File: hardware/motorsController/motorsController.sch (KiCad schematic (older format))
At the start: 12 parts, among them J1 batery_connector, J10 batery_connector, J11 Conn_01x04, J2 Screw_Terminal_01x01, J3 Screw_Terminal_01x01, J4 Screw_Terminal_01x01, J5 Screw_Terminal_01x01, J6 Screw_Terminal_01x01, J7 Screw_Terminal_01x01, J8 Screw_Terminal_01x01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

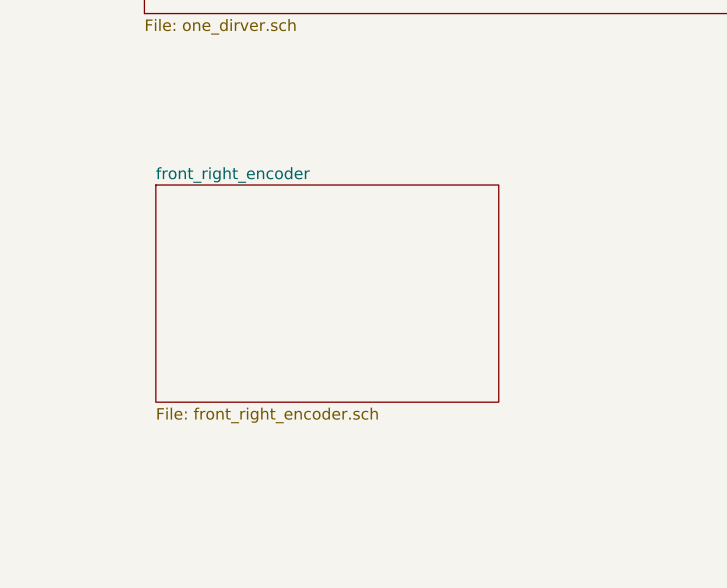
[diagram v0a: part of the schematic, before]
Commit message: layout filters for an encoder
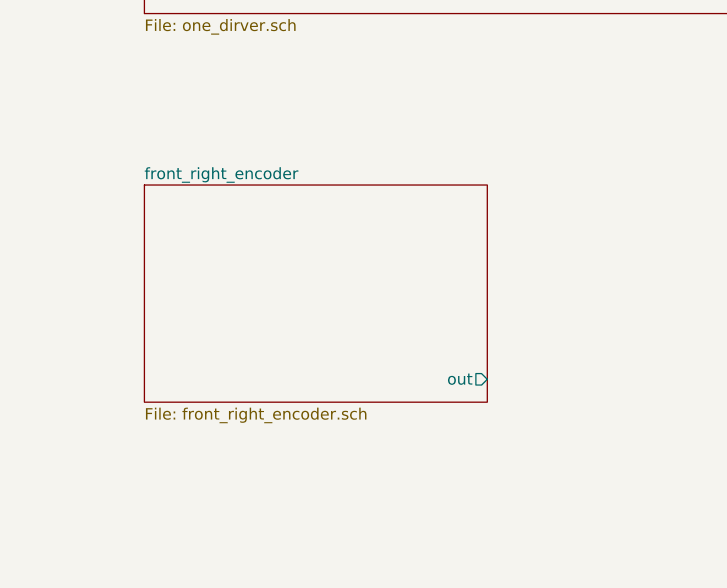
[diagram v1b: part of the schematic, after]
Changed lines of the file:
@@
 $EndComp
 $Sheet
-S 1300 6400 1500 950
+S 1250 6400 1500 950
 U 5FB03879
 F0 "front_right_encoder" 50
 F1 "front_right_encoder.sch" 50
+F2 "out" O R 2750 7250 50
 $EndSheet
 $EndSCHEMATC

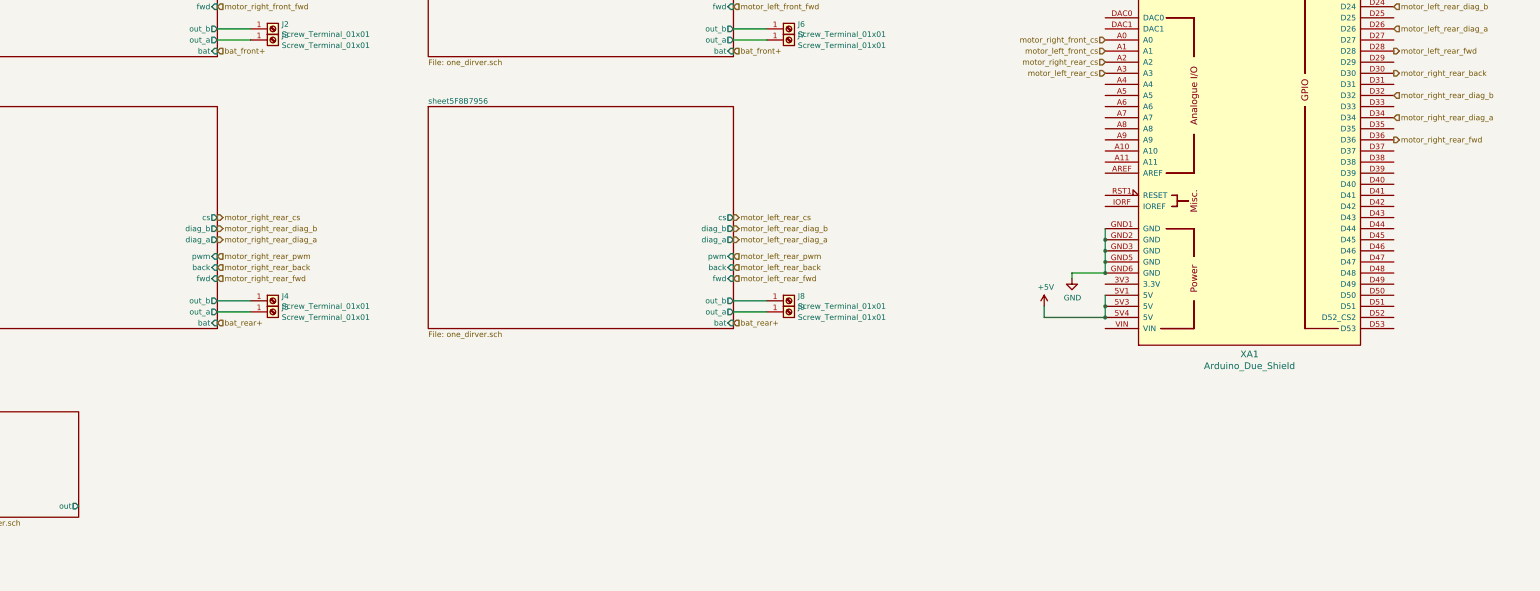
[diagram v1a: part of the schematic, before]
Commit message: connect encoder to arduino
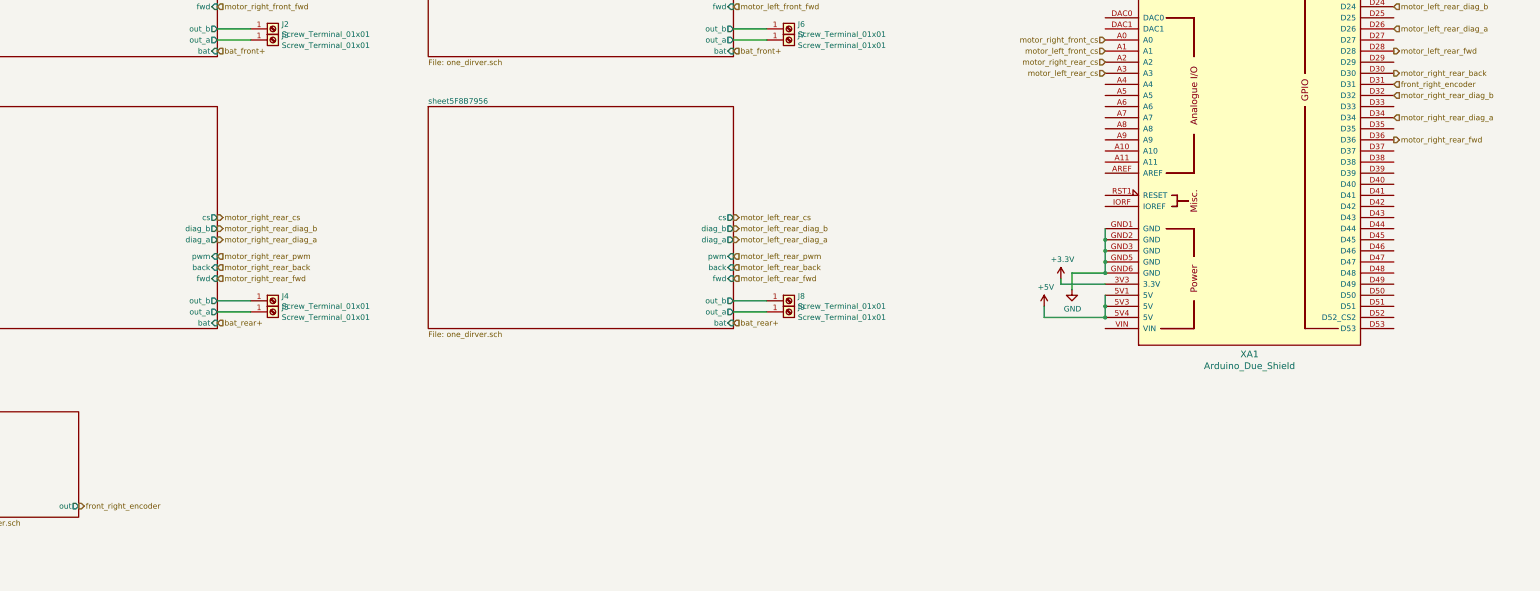
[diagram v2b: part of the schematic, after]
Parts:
- J11: footprint Connector_PinHeader_1.00mm:PinHeader_1x04_P1.00mm_Vertical -> Connector_PinSocket_2.54mm:PinSocket_1x04_P2.54mm_Vertical
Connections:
- net +3V3: now reaches XA1.3V3 (3.3V)
- net front_right_encoder: now reaches XA1.D31
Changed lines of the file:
@@
 L power:GND #PWR0105
 U 1 1 5F7FA8F7
-P 11700 5200
-F 0 "#PWR0105" H 11700 4950 50  0001 C CNN
-F 1 "GND" H 11705 5027 50  0000 C CNN
-F 2 "" H 11700 5200 50  0001 C CNN
-F 3 "" H 11700 5200 50  0001 C CNN
-	1    11700 5200
-	1    0    0    -1
-$EndComp
-Wire Wire Line
-	11700 5200 11700 5150
+P 11700 5300
+F 0 "#PWR0105" H 11700 5050 50  0001 C CNN
+F 1 "GND" H 11705 5127 50  0000 C CNN
+F 2 "" H 11700 5300 50  0001 C CNN
+F 3 "" H 11700 5300 50  0001 C CNN
+	1    11700 5300
+	1    0    0    -1
+$EndComp
+Wire Wire Line
+	11700 5300 11700 5150
 Wire Wire Line
 	11700 5150 12000 5150
@@
 F 0 "J11" H 918 9275 50  0000 C CNN
 F 1 "Conn_01x04" H 918 9366 50  0000 C CNN
-F 2 "Connector_PinHeader_1.00mm:PinHeader_1x04_P1.00mm_Vertical" H 1000 9700 50  0001 C CNN
+F 2 "Connector_PinSocket_2.54mm:PinSocket_1x04_P2.54mm_Vertical" H 1000 9700 50  0001 C CNN
 F 3 "~" H 1000 9700 50  0001 C CNN
 	1    1000 9700
@@
 F2 "out" O R 2750 7250 50
 $EndSheet
+$Comp
+L power:+3.3V #PWR0128
+U 1 1 5FBBD825
+P 11600 5200
+F 0 "#PWR0128" H 11600 5050 50  0001 C CNN
+F 1 "+3.3V" H 11615 5373 50  0000 C CNN
+F 2 "" H 11600 5200 50  0001 C CNN
+F 3 "" H 11600 5200 50  0001 C CNN
+	1    11600 5200
+	1    0    0    -1
+$EndComp
+Wire Wire Line
+	11600 5200 11600 5250
+Wire Wire Line
+	11600 5250 12000 5250
+Text HLabel 2750 7250 2    50   Output ~ 0
+front_right_encoder
+Text HLabel 14600 3450 2    50   Input ~ 0
+front_right_encoder
 $EndSCHEMATC

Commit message: add three more encoders
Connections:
- net front_left_encoder: now reaches XA1.D33
- net rear_right_encoder: now reaches XA1.D35
- net rear_left_encoder: now reaches XA1.D37
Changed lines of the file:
@@
 $Descr A3 16535 11693
 encoding utf-8
-Sheet 1 6
+Sheet 1 9
 Title ""
 Date ""
@@
 Text HLabel 14600 3450 2    50   Input ~ 0
 front_right_encoder
+$Sheet
+S 3650 6400 1500 950
+U 5FBFC472
+F0 "front_left_encoder" 50
+F1 "front_right_encoder.sch" 50
+F2 "out" O R 5150 7250 50
+$EndSheet
+Text HLabel 5150 7250 2    50   Output ~ 0
+front_left_encoder
+Text HLabel 14600 3650 2    50   Input ~ 0
+front_left_encoder
+$Sheet
+S 1250 7750 1500 950
+U 5FC04BEE
+F0 "rear_right_encoder" 50
+F1 "front_right_encoder.sch" 50
+F2 "out" O R 2750 8600 50
+$EndSheet
+Text HLabel 2750 8600 2    50   Output ~ 0
+rear_right_encoder
+$Sheet
+S 3650 7750 1500 950
+U 5FC04BF2
+F0 "rear_left_encoder" 50
+F1 "front_right_encoder.sch" 50
+F2 "out" O R 5150 8600 50
+$EndSheet
+Text HLabel 5150 8600 2    50   Output ~ 0
+rear_left_encoder
+Text HLabel 14600 3850 2    50   Input ~ 0
+rear_right_encoder
+Text HLabel 14600 4050 2    50   Input ~ 0
+rear_left_encoder
 $EndSCHEMATC

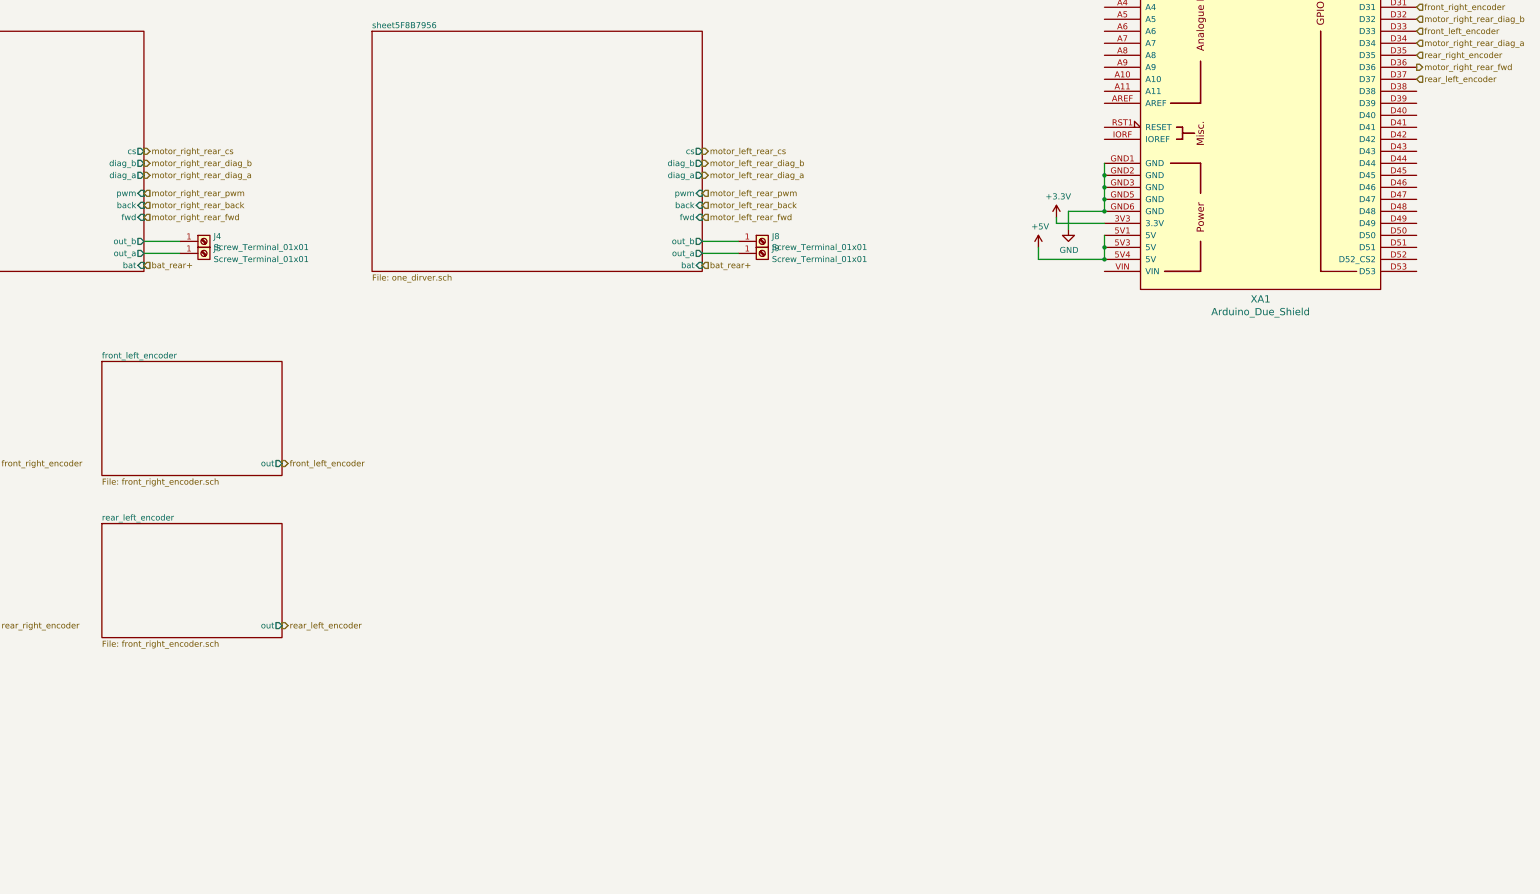
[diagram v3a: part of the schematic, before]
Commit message: add indication leds to schematics
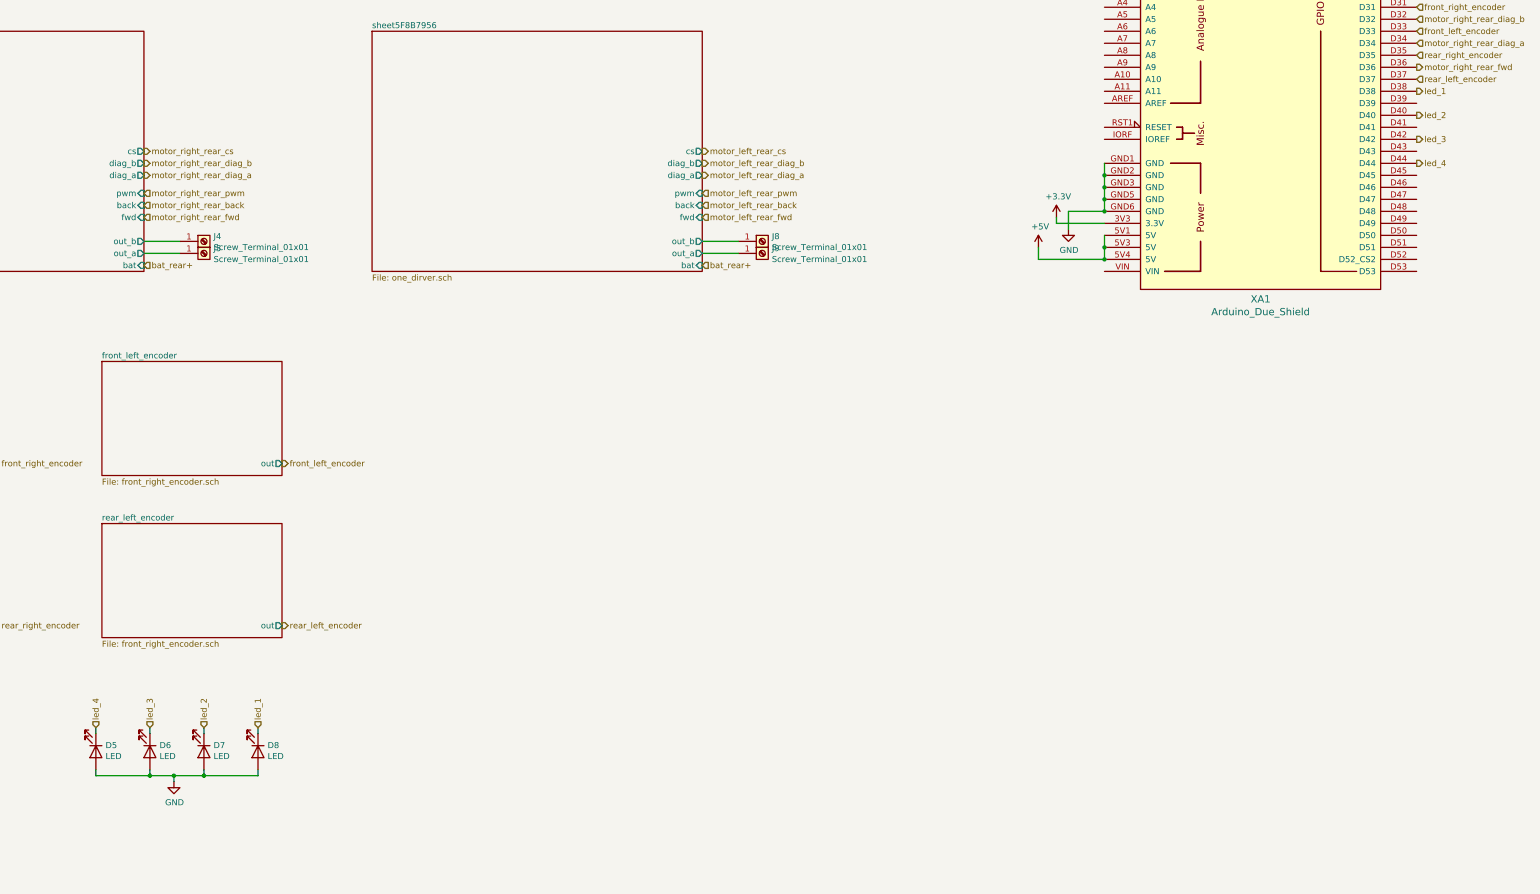
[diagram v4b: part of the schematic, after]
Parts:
- added D5, D6, D7, D8: LED, symbol Device:LED
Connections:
- net GND: now also D5.2 (A), D6.2 (A), D7.2 (A), D8.2 (A)
- net led_1: now reaches XA1.D38
- net led_1: now also D8.1 (K)
- net led_2: now reaches XA1.D40
- net led_2: now also D7.1 (K)
- net led_3: now reaches XA1.D42
- net led_3: now also D6.1 (K)
- net led_4: now reaches XA1.D44
- net led_4: now also D5.1 (K)
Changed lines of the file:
@@
 Text HLabel 14600 4050 2    50   Input ~ 0
 rear_left_encoder
+$Comp
+L Device:LED D5
+U 1 1 5FC19CB9
+P 3600 9650
+F 0 "D5" V 3547 9730 50  0000 L CNN
+F 1 "LED" V 3638 9730 50  0000 L CNN
+F 2 "" H 3600 9650 50  0001 C CNN
+F 3 "~" H 3600 9650 50  0001 C CNN
+	1    3600 9650
+	0    1    1    0
+$EndComp
+$Comp
+L Device:LED D6
+U 1 1 5FC1D350
+P 4050 9650
+F 0 "D6" V 3997 9730 50  0000 L CNN
+F 1 "LED" V 4088 9730 50  0000 L CNN
+F 2 "" H 4050 9650 50  0001 C CNN
+F 3 "~" H 4050 9650 50  0001 C CNN
+	1    4050 9650
+	0    1    1    0
+$EndComp
+$Comp
+L Device:LED D7
+U 1 1 5FC1DB12
+P 4500 9650
+F 0 "D7" V 4447 9730 50  0000 L CNN
+F 1 "LED" V 4538 9730 50  0000 L CNN
+F 2 "" H 4500 9650 50  0001 C CNN
+F 3 "~" H 4500 9650 50  0001 C CNN
+	1    4500 9650
+	0    1    1    0
+$EndComp
+$Comp
+L Device:LED D8
+U 1 1 5FC1E600
+P 4950 9650
+F 0 "D8" V 4897 9730 50  0000 L CNN
+F 1 "LED" V 4988 9730 50  0000 L CNN
+F 2 "" H 4950 9650 50  0001 C CNN
+F 3 "~" H 4950 9650 50  0001 C CNN
+	1    4950 9650
+	0    1    1    0
+$EndComp
+Wire Wire Line
+	3600 9500 3600 9450
+Wire Wire Line
+	4950 9450 4950 9500
+Wire Wire Line
+	4500 9500 4500 9450
+Wire Wire Line
+	4050 9500 4050 9450
+Wire Wire Line
+	3600 9800 3600 9850
+Wire Wire Line
+	3600 9850 4050 9850
+Wire Wire Line
+	4950 9850 4950 9800
+Wire Wire Line
+	4500 9850 4500 9800
+Connection ~ 4500 9850
+Wire Wire Line
+	4500 9850 4950 9850
+Wire Wire Line
+	4050 9800 4050 9850
+Connection ~ 4050 9850
+Wire Wire Line
+	4050 9850 4250 9850
+$Comp
+L power:GND #PWR01
+U 1 1 5FC28A45
+P 4250 9900
+F 0 "#PWR01" H 4250 9650 50  0001 C CNN
+F 1 "GND" H 4255 9727 50  0000 C CNN
+F 2 "" H 4250 9900 50  0001 C CNN
+F 3 "" H 4250 9900 50  0001 C CNN
+	1    4250 9900
+	1    0    0    -1
+$EndComp
+Wire Wire Line
+	4250 9900 4250 9850
+Connection ~ 4250 9850
+Wire Wire Line
+	4250 9850 4500 9850
+Text HLabel 4950 9450 1    50   Input ~ 0
+led_1
+Text HLabel 4500 9450 1    50   Input ~ 0
+led_2
+Text HLabel 4050 9450 1    50   Input ~ 0
+led_3
+Text HLabel 3600 9450 1    50   Input ~ 0
+led_4
+Text HLabel 14600 4150 2    50   Output ~ 0
+led_1
+Text HLabel 14600 4550 2    50   Output ~ 0
+led_3
+Text HLabel 14600 4750 2    50   Output ~ 0
+led_4
+Text HLabel 14600 4350 2    50   Output ~ 0
+led_2
 $EndSCHEMATC

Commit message: layout indicator leds on a pcb
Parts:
- D5, D6, D7, D8: footprint (none) -> LED_SMD:LED_0805_2012Metric
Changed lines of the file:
@@
 F 0 "D5" V 3547 9730 50  0000 L CNN
 F 1 "LED" V 3638 9730 50  0000 L CNN
-F 2 "" H 3600 9650 50  0001 C CNN
+F 2 "LED_SMD:LED_0805_2012Metric" H 3600 9650 50  0001 C CNN
 F 3 "~" H 3600 9650 50  0001 C CNN
 	1    3600 9650
@@
 F 0 "D6" V 3997 9730 50  0000 L CNN
 F 1 "LED" V 4088 9730 50  0000 L CNN
-F 2 "" H 4050 9650 50  0001 C CNN
+F 2 "LED_SMD:LED_0805_2012Metric" H 4050 9650 50  0001 C CNN
 F 3 "~" H 4050 9650 50  0001 C CNN
 	1    4050 9650
@@
 F 0 "D7" V 4447 9730 50  0000 L CNN
 F 1 "LED" V 4538 9730 50  0000 L CNN
-F 2 "" H 4500 9650 50  0001 C CNN
+F 2 "LED_SMD:LED_0805_2012Metric" H 4500 9650 50  0001 C CNN
 F 3 "~" H 4500 9650 50  0001 C CNN
 	1    4500 9650
@@
 F 0 "D8" V 4897 9730 50  0000 L CNN
 F 1 "LED" V 4988 9730 50  0000 L CNN
-F 2 "" H 4950 9650 50  0001 C CNN
+F 2 "LED_SMD:LED_0805_2012Metric" H 4950 9650 50  0001 C CNN
 F 3 "~" H 4950 9650 50  0001 C CNN
 	1    4950 9650

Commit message: remove old motorsController; create a draft schematic for an H-bridge
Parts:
- removed D5, D6, D7, D8: LED, LED_SMD:LED_0805_2012Metric, symbol Device:LED
- removed J1, J10: batery_connector, TerminalBlock:TerminalBlock_bornier-2_P5.08mm, symbol Connector:Screw_Terminal_01x02
- removed J11: Conn_01x04, Connector_PinSocket_2.54mm:PinSocket_1x04_P2.54mm_Vertical, symbol Connector_Generic:Conn_01x04
- removed J2, J3, J4, J5, J6, J7, J8, J9: Screw_Terminal_01x01, Connector_Pin:Pin_D1.3mm_L11.3mm_W2.8mm_Flat, symbol Connector:Screw_Terminal_01x01
- removed XA1: Arduino_Due_Shield, Arduino:Arduino_Due_Shield, symbol arduino:Arduino_Due_Shield
- added C? (x2): CP1, symbol Device:CP1
- added D? (x2): D, symbol Device:D
- added M?: Motor_DC, symbol Motor:Motor_DC
- added Q? (x5): IRF540NSTRLPBF, TO254P1524X483-3N, symbol IRF540NSTRLPBF:IRF540NSTRLPBF
- added R? (x4): R, symbol Device:R
- added U? (x2): IR2011, symbol Driver_FET:IR2011
- added U? (x2): CPC-5002, Package_DIP:DIP-8_W7.62mm, symbol Isolator:CPC-5002
- added U?: FAN3100TSX, ON_Semi-527AH-0-0-*, symbol eec:FAN3100TSX
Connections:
- net +5V: now also D?.2 (A), D?.2 (A), U?.1 (VCC), U?.1 (VCC), U?.8 (VCC), U?.8 (VCC)
- net GND: now also U?.2 (C1), U?.2 (C1), U?.3 (C2), U?.3 (C2)
- new net: Q?.1, R?.1 (x4)
- new net: C?.2, M?.2 (-), Q?.2, Q?.3, U?.4 (VS)
- new net: Q?.2, Q?.3, Q?.3, U?.7 (COM), U?.7 (COM)
- new net: C?.2, M?.1 (+), Q?.2, Q?.3, U?.4 (VS)
- new net: C?.1, D?.1 (K), U?.2 (VB) (x2)
- new net: R?.2, U?.3 (HO) (x2)
- new net: U?.5 (HIN), U?.7 (VO1) (x2)
- new net: U?.6 (LIN), U?.6 (VO2) (x2)
- new net: R?.2, U?.8 (LO) (x2)
- new net: Q?.1, U?.5 (OUT)
- new net +12C: U?.1 (VDD)
- new net +12V: Q?.2, Q?.2
- new net AD: U?.1 (A1), U?.4 (A2)
- new net BC: U?.1 (A1), U?.4 (A2)
- new net GNDPWR: Q?.3, U?.2 (GND), U?.4 (IN−), U?.5 (GND), U?.5 (GND)
- new net PWM: U?.3 (IN+)
- no-connect marks 6 -> 0
